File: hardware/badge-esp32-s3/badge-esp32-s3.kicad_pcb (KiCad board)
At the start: 2 copper layers, 127 x 76 mm, 0 parts

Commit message: Finish schematic, start placing parts on layout
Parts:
- added BUZZER1: MLT-5020, lcsc-lib:BUZ-SMD_L5.0-W5.5-P4.60, F.Cu at (179.0, 79.0)
- added C1: 10uF, PCM_JLCPCB:C_0603, F.Cu at (-92.3, 87.6)
- added C10: 100nF, PCM_JLCPCB:C_0603, F.Cu at (-83.7, 142.7)
- added C11: 100nF, PCM_JLCPCB:C_0603, F.Cu at (-92.3, 142.7)
- added C12: 10uF, PCM_JLCPCB:C_0603, F.Cu at (-36.4, 112.4)
- added C13: 10uF, PCM_JLCPCB:C_0603, F.Cu at (-36.4, 114.7)
- added C14: 100nF, PCM_JLCPCB:C_0603, F.Cu at (-69.2, 140.2)
- added C15: 1uF, PCM_JLCPCB:C_0402, F.Cu at (-46.6, 115.5)
- added C16: 1uF, PCM_JLCPCB:C_0402, F.Cu at (-46.6, 117.4)
- added C17: 1uF, PCM_JLCPCB:C_0402, F.Cu at (-46.6, 119.2)
- added C18: 1uF, PCM_JLCPCB:C_0603, F.Cu at (-8.72, 58.6)
- added C19: 1uF, PCM_JLCPCB:C_0603, F.Cu at (-9.82, 126.2)
- added C2: 100nF, PCM_JLCPCB:C_0603, F.Cu at (-92.3, 89.8)
- added C20: 1uF, PCM_JLCPCB:C_0603, F.Cu at (-10.7, 101.4)
- added C21: 1uF, PCM_JLCPCB:C_0603, F.Cu at (-45.8, 130.6)
- added C22: 1uF, PCM_JLCPCB:C_0603, F.Cu at (-8.72, 73.7)
- added C23: 1uF, PCM_JLCPCB:C_0603, F.Cu at (-9.82, 140.0)
- added C24: 100nF, PCM_JLCPCB:C_0603, F.Cu at (-14.5, 81.6)
- added C25: 100nF, PCM_JLCPCB:C_0603, F.Cu at (-14.5, 83.9)
- added C26: 4.7uF, PCM_JLCPCB:C_0603, F.Cu at (-14.5, 86.1)
- added C3: 1uF, PCM_JLCPCB:C_0402, F.Cu at (-44.4, 83.6)
- added C4: 1uF, PCM_JLCPCB:C_0402, F.Cu at (-44.4, 85.4)
- added C5: 10uF, PCM_JLCPCB:C_0603, F.Cu at (-22.6, 75.9)
- added C6: 10uF, PCM_JLCPCB:C_0603, F.Cu at (-22.6, 60.7)
- added C7: 10uF, PCM_JLCPCB:C_0603, F.Cu at (-36.8, 60.5)
- added C8: 1uF, PCM_JLCPCB:C_0402, F.Cu at (-44.4, 51.1)
- added C9: 1uF, PCM_JLCPCB:C_0402, F.Cu at (-44.4, 52.9)
- added CN1: B4B-PH-SM4-TB (LF)(SN), lcsc-lib:CONN-SMD_B4B-PH-SM4-TB-LF-SN, F.Cu at (-54.8, 112.8)
- added Card1: TF PUSH, lcsc-lib:TF-SMD_TF-PUSH, F.Cu at (152.9, 131.3)
- added D1: Red, PCM_JLCPCB:D_0603, F.Cu at (-40.9, 84.0)
- added D10: Red, PCM_JLCPCB:D_0603, F.Cu at (-46.5, 142.0)
- added D11: B0520W, PCM_JLCPCB:D_SOD-123, F.Cu at (-21.9, 102.7)
- added D12: Green, PCM_JLCPCB:D_0805, F.Cu at (-21.6, 112.3)
- added D2: LESD5D5.0CT1G, lcsc-lib:SOD-523_L1.2-W0.8-LS1.6-BI, F.Cu at (-17.9, 66.4)
- added D3: LESD5D5.0CT1G, lcsc-lib:SOD-523_L1.2-W0.8-LS1.6-BI, F.Cu at (-17.9, 68.5)
- added D4: LESD5D5.0CT1G, lcsc-lib:SOD-523_L1.2-W0.8-LS1.6-BI, F.Cu at (-17.9, 70.6)
- added D5: B0520W, PCM_JLCPCB:D_SOD-123, F.Cu at (-27.4, 76.5)
- added D6: LESD5D5.0CT1G, lcsc-lib:SOD-523_L1.2-W0.8-LS1.6-BI, F.Cu at (-17.9, 51.2)
- added D7: LESD5D5.0CT1G, lcsc-lib:SOD-523_L1.2-W0.8-LS1.6-BI, F.Cu at (-17.9, 53.3)
- added D8: LESD5D5.0CT1G, lcsc-lib:SOD-523_L1.2-W0.8-LS1.6-BI, F.Cu at (-17.9, 55.5)
- added D9: B0520W, PCM_JLCPCB:D_SOD-123, F.Cu at (-27.4, 61.3)
- added J1: Connector, USB-TYPE-C-16P, PCM_JLCPCB:TYPE-C-SMD_HX-TYPE-C-16PIN, F.Cu at (122.5, 69.0)
- added J2: Connector, USB-TYPE-C-16P, PCM_JLCPCB:TYPE-C-SMD_HX-TYPE-C-16PIN, F.Cu at (179.0, 69.0)
- added J3: ~, lcsc-lib:FPC-SMD_AFC01-S12FCA-00, F.Cu at (122.2, 101.5)
- added LED1: RS-3535MWAM, lcsc-lib:LED-ARRAY-SMD_L3.7-W3.5-P1.10-TL, F.Cu at (169.0, 80.0)
- added MB1: MiniBadge_Full, minibadge:MiniBadge_Full_NoEdges, F.Cu at (87.2, 65.7)
- added MB2: MiniBadge_Full, minibadge:MiniBadge_Full_NoEdges, F.Cu at (192.7, 65.7)
- added P1: PH-2A_C2319, lcsc-lib:CONN-TH_2P-P2.00_PH-2A_C2319, F.Cu at (89.0, 93.0)
- added Q1: SS8050 200-350, PCM_JLCPCB:Q_SOT-23, F.Cu at (-34.8, 52.5)
- added Q2: SS8050 200-350, PCM_JLCPCB:Q_SOT-23, F.Cu at (-34.8, 57.2)
- added Q3: HL2301A, PCM_JLCPCB:Q_SOT-23, F.Cu at (-26.3, 113.2)
- added R1: 0Ω, PCM_JLCPCB:R_0402, F.Cu at (-89.0, 87.4)
- added R10: 10kΩ, PCM_JLCPCB:R_0402, F.Cu at (-41.5, 51.1)
- added R11: 0Ω, PCM_JLCPCB:R_0402, F.Cu at (-41.5, 52.9)
- added R12: 0Ω, PCM_JLCPCB:R_0402, F.Cu at (-41.5, 54.8)
- added R13: 10kΩ, PCM_JLCPCB:R_0402, F.Cu at (-41.5, 56.6)
- added R14: 10kΩ, PCM_JLCPCB:R_0402, F.Cu at (-41.5, 58.5)
- added R15: 0Ω, PCM_JLCPCB:R_0402, F.Cu at (-38.7, 51.1)
- added R16: 0Ω, PCM_JLCPCB:R_0402, F.Cu at (-38.7, 52.9)
- added R17: 10kΩ, PCM_JLCPCB:R_0402, F.Cu at (-38.7, 54.8)
- added R18: 100Ω, PCM_JLCPCB:R_0402, F.Cu at (-28.9, 89.0)
- added R19: 5.1kΩ, PCM_JLCPCB:R_0402, F.Cu at (-50.0, 136.9)
- added R2: 5.1kΩ, PCM_JLCPCB:R_0402, F.Cu at (-44.4, 87.3)
- added R20: 100Ω, PCM_JLCPCB:R_0402, F.Cu at (-50.0, 138.7)
- added R21: 47Ω, PCM_JLCPCB:R_0402, F.Cu at (-50.0, 140.6)
- added R22: 47Ω, PCM_JLCPCB:R_0402, F.Cu at (-50.0, 142.4)
- added R23: 3296W-1-103, lcsc-lib:RES-ADJ-TH_3P-L10.0-W10.0-P2.50-L, F.Cu at (187.5, 78.5)
- added R24: 100kΩ, PCM_JLCPCB:R_0402, F.Cu at (-20.2, 105.7)
- added R25: 1kΩ, PCM_JLCPCB:R_0402, F.Cu at (-20.2, 107.6)
- added R26: 2.2kΩ, PCM_JLCPCB:R_0402, F.Cu at (-20.2, 109.4)
- added R27: 10kΩ, PCM_JLCPCB:R_0603, F.Cu at (-12.5, 58.6)
- added R28: 10kΩ, PCM_JLCPCB:R_0603, F.Cu at (-12.5, 60.8)
- added R29: 10kΩ, PCM_JLCPCB:R_0603, F.Cu at (-13.6, 126.2)
- added R3: 5.1kΩ, PCM_JLCPCB:R_0402, F.Cu at (-19.3, 75.7)
- added R30: 10kΩ, PCM_JLCPCB:R_0603, F.Cu at (-13.6, 128.5)
- added R31: 10kΩ, PCM_JLCPCB:R_0603, F.Cu at (-14.5, 101.4)
- added R32: 10kΩ, PCM_JLCPCB:R_0603, F.Cu at (-14.5, 103.6)
- added R33: 10kΩ, PCM_JLCPCB:R_0603, F.Cu at (-49.6, 130.6)
- added R34: 10kΩ, PCM_JLCPCB:R_0603, F.Cu at (-49.6, 132.8)
- added R35: 10kΩ, PCM_JLCPCB:R_0603, F.Cu at (-12.5, 73.7)
- added R36: 10kΩ, PCM_JLCPCB:R_0603, F.Cu at (-12.5, 76.0)
- added R37: 10kΩ, PCM_JLCPCB:R_0603, F.Cu at (-13.6, 140.0)
- added R38: 10kΩ, PCM_JLCPCB:R_0603, F.Cu at (-13.6, 142.3)
- added R39: 4.7kΩ, PCM_JLCPCB:R_0603, F.Cu at (-10.8, 85.9)
- added R4: 5.1kΩ, PCM_JLCPCB:R_0402, F.Cu at (-19.3, 77.6)
- added R40: 4.7kΩ, PCM_JLCPCB:R_0603, F.Cu at (-10.8, 88.2)
- added R5: 5.1kΩ, PCM_JLCPCB:R_0402, F.Cu at (-19.3, 60.5)
- added R6: 5.1kΩ, PCM_JLCPCB:R_0402, F.Cu at (-19.3, 62.4)
- added R7: 22kΩ, PCM_JLCPCB:R_0402, F.Cu at (-44.4, 54.8)
- added R8: 47kΩ, PCM_JLCPCB:R_0402, F.Cu at (-44.4, 56.6)
- added R9: 1kΩ, PCM_JLCPCB:R_0402, F.Cu at (-44.4, 58.5)
- added S1: 2765, AdafruitJoystick:SW_2765, F.Cu at (98.5, 107.5)
- added SW1: TS-1088-AR02016, lcsc-lib:SW-SMD_L3.9-W3.0-P4.45, F.Cu at (133.5, 72.0)
- added SW2: TS-1088-AR02016, lcsc-lib:SW-SMD_L3.9-W3.0-P4.45, F.Cu at (164.5, 72.0)
- added SW3: SK-12F04-G050, lcsc-lib:SW-TH_G-SWITCH_SK-12F04-G050, F.Cu at (210.5, 96.5)
- added SW4: TS665CJ, lcsc-lib:SW-TH_4P-L6.0-W6.0-P4.50-LS6.5, F.Cu at (206.0, 123.5)
- added SW5: TS665CJ, lcsc-lib:SW-TH_4P-L6.0-W6.0-P4.50-LS6.5, F.Cu at (197.2, 115.5)
- added SW6: TS665CJ, lcsc-lib:SW-TH_4P-L6.0-W6.0-P4.50-LS6.5, F.Cu at (189.0, 123.8)
- added SW7: TS665CJ, lcsc-lib:SW-TH_4P-L6.0-W6.0-P4.50-LS6.5, F.Cu at (111.8, 129.8)
- added SW8: TS665CJ, lcsc-lib:SW-TH_4P-L6.0-W6.0-P4.50-LS6.5, F.Cu at (99.2, 126.2)
- added SW9: TS665CJ, lcsc-lib:SW-TH_4P-L6.0-W6.0-P4.50-LS6.5, F.Cu at (197.5, 132.0)
- added U1: ESP32-S3-MINI-1-N8, RF_Module:ESP32-S2-MINI-1, F.Cu at (150.7, 75.5)
- added U10: FH2.54-09-02PZD, lcsc-lib:HDR-TH_2P-P2.54-V-M-5, F.Cu at (-66.3, 102.7)
- added U11: FH2.54-09-04PZD, lcsc-lib:HDR-TH_4P-P2.54-V-F, F.Cu at (-55.6, 94.8)
- added U12: FH2.54-09-03PZD, lcsc-lib:HDR-TH_3P-P2.54-V-F, F.Cu at (-45.0, 102.3)
- added U13: FH2.54-09-02PZD, lcsc-lib:HDR-TH_2P-P2.54-V-M-5, F.Cu at (-109.0, 104.0)
- added U14: FH2.54-09-04PZD, lcsc-lib:HDR-TH_4P-P2.54-V-F, F.Cu at (-55.6, 98.6)
- added U15: FH2.54-09-04PZD, lcsc-lib:HDR-TH_4P-P2.54-V-F, F.Cu at (-55.6, 102.4)
- added U16: FH2.54-09-04PZD, lcsc-lib:HDR-TH_4P-P2.54-V-F, F.Cu at (-55.6, 106.2)
- added U17: FH2.54-09-02PZD, lcsc-lib:HDR-TH_2P-P2.54-V-M-5, F.Cu at (-11.5, 110.0)
- added U18: MMA8452QR1_C11360, lcsc-lib:QFN-16_L3.0-W3.0-P0.50-TL_MMA8452QR1, F.Cu at (198.5, 93.8)
- added U19: FH2.54-09-02PZD, lcsc-lib:HDR-TH_2P-P2.54-V-M-5, F.Cu at (-66.3, 115.7)
- added U2: NCP167BMX330TBG, lcsc-lib:XDFN-4_L1.0-W1.0-P0.65-BL-EP, F.Cu at (-41.4, 86.5)
- added U3: CP2102N-A02-GQFN28R, lcsc-lib:QFN-28_L5.0-W5.0-P0.50-TL-EP3.3, F.Cu at (122.1, 78.5)
- added U4: TP4056, PCM_JLCPCB:ESOP-8_L4.9-W3.9-P1.27-LS6.0-BL-EP, F.Cu at (102.8, 93.0)
- added U5: FH2.54-09-02PZD, lcsc-lib:HDR-TH_2P-P2.54-V-M-5, F.Cu at (-28.3, 131.0)
- added U6: ZX-SH1.0-4PWT, lcsc-lib:CONN-SMD_4P-P1.00_MEGASTAR_ZX-SH1.0-4PWT, F.Cu at (-44.2, 111.2)
- added U7: FH2.54-09-02PZD, lcsc-lib:HDR-TH_2P-P2.54-V-M-5, F.Cu at (-90.8, 113.5)
- added U8: FH2.54-09-03PZD, lcsc-lib:HDR-TH_3P-P2.54-V-F, F.Cu at (-45.0, 94.8)
- added U9: FH2.54-09-03PZD, lcsc-lib:HDR-TH_3P-P2.54-V-F, F.Cu at (-45.0, 98.6)

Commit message: Layout placed
I've completed the PCB layout and am handing it off for trace routing. It's been a while since I last did this, so while I did my best to optimize placement, there may be areas where space is tight. Feel free to adjust component positioning as needed to make routing easier.

Feedback is welcome—I wish I had more time to do the traces myself since that would be a valuable learning opportunit.
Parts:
- moved C3 250.9 mm to (206.4, 91.1), turned to -90 degrees
- moved C4 248.0 mm to (203.5, 93.2)
- moved R2 245.8 mm to (201.4, 91.1), turned to 90 degrees
- moved U2 244.9 mm to (203.5, 91.1)
- moved D1 244.5 mm to (203.6, 88.6), turned to 180 degrees
- moved U13 241.2 mm to (129.8, 137.7)
- moved C11 239.3 mm to (137.8, 77.0), turned to 90 degrees
- moved U12 234.3 mm to (189.3, 103.3), turned to 90 degrees
- moved U19 234.0 mm to (164.6, 77.7), turned to 180 degrees
- moved C10 232.4 mm to (137.8, 72.4), turned to 90 degrees
- moved U7 231.0 mm to (138.9, 137.7), turned to 180 degrees
- moved U9 228.8 mm to (183.8, 103.2), turned to 90 degrees
- moved U11 228.7 mm to (173.0, 102.1), turned to 90 degrees
- moved C14 227.6 mm to (157.8, 123.6)
- moved R28 225.5 mm to (205.4, 119.0), turned to 180 degrees
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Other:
- board outline removed

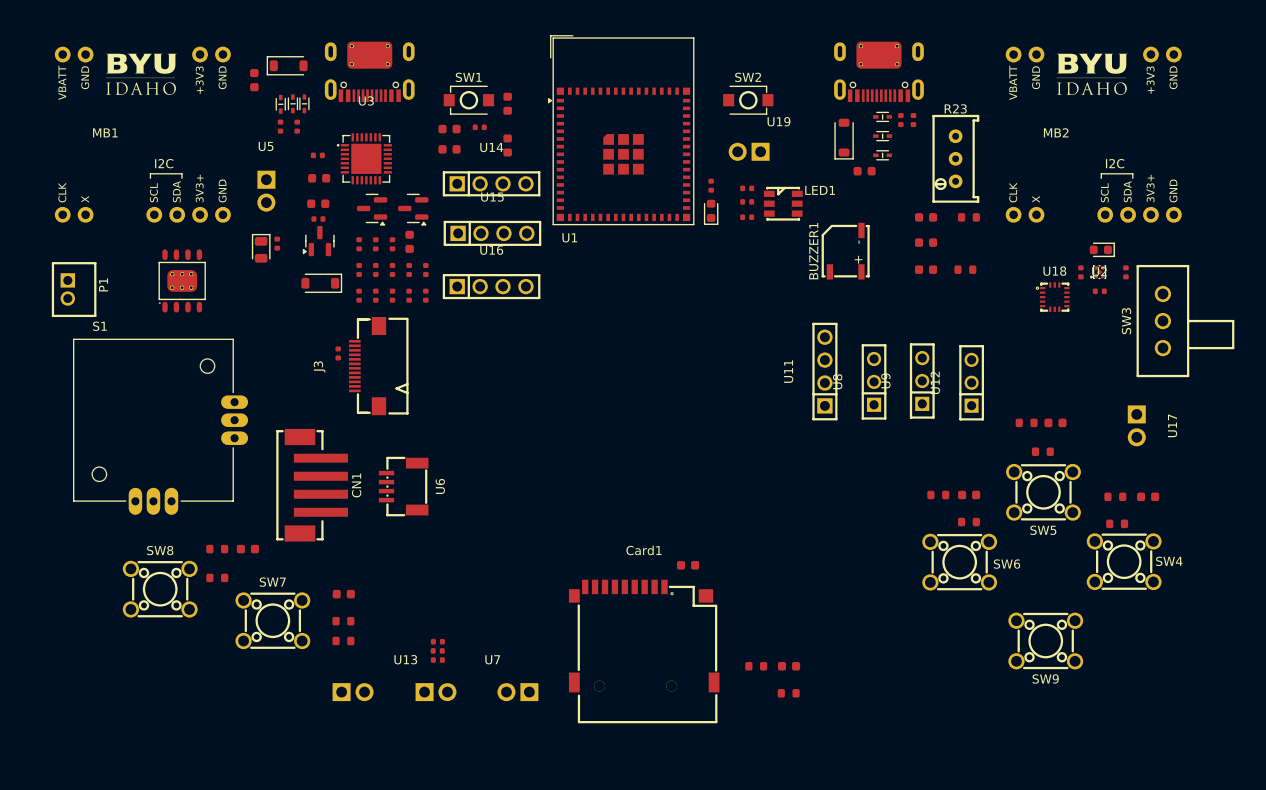
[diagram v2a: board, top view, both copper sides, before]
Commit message: Add nice silkscreens
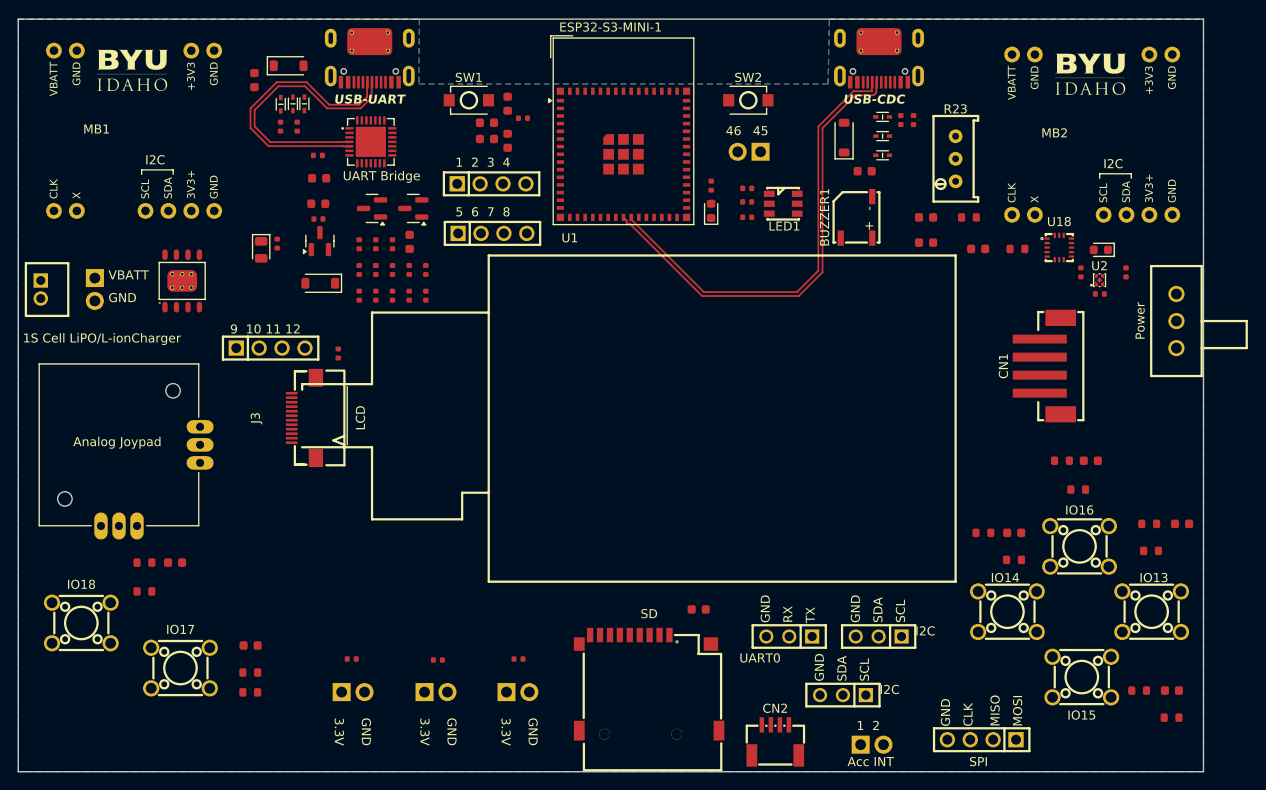
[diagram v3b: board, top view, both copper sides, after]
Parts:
- added LCD: OLED-SMD_HS20HS072RX, lcsc-lib:OLED-SMD_HS20HS072RX, F.Cu at (117.5, 107.2)
- moved CN1 83.1 mm to (198.0, 101.5), turned to 90 degrees
- moved CN2 50.1 mm to (167.5, 143.0), turned to 0 degrees
- moved U17 46.0 mm to (178.2, 143.5), turned to 0 degrees
- moved U11 44.4 mm to (190.4, 142.9), turned to 180 degrees
- moved R37 42.6 mm to (207.9, 137.5)
- moved R38 42.6 mm to (211.5, 140.5)
- moved C23 42.6 mm to (211.5, 137.5)
- moved U9 35.9 mm to (175.0, 138.0), turned to 180 degrees
- moved U12 30.0 mm to (179.0, 131.5), turned to 180 degrees
- moved U8 29.8 mm to (169.0, 131.5), turned to 180 degrees
- moved U16 25.4 mm to (111.5, 99.5)
- moved U5 21.9 mm to (92.0, 93.0)
- moved C21 11.8 mm to (109.3, 132.5)
- moved R33 11.8 mm to (109.2, 137.7)
- moved R34 11.8 mm to (109.2, 135.5)
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- renumbered U6 to CN2, SW4 to IO13, SW6 to IO14, SW9 to IO15, SW5 to IO16, SW7 to IO17, SW8 to IO18, SW3 to Power, Card1 to SD
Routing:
- net /ESP_USB-: track 0.00 -> 51.8 mm
- net /ESP_USB+: track 0.00 -> 49.9 mm
- net /UART Interface/USB_DN: track 0.00 -> 31.2 mm
- net /UART Interface/USB_DP: track 0.00 -> 30.4 mm
- added copper zone on B.Cu, net GND
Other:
- board outline added: 131.5 x 83.5 mm
- board text added: "1 2"
- board text added: "1 2 3 4"
- board text added: "1S Cell LiPO/L-ionCharger"
- board text added: "3.3V"
- board text added: "45"
- board text added: "46"
- board text added: "5 6 7 8"
- board text added: "9 10 11 12"
- board text added: "Acc INT"
- board text added: "Analog Joypad"
- board text added: "CLK"
- board text added: "ESP32-S3-MINI-1"
- board text added: "GND"
- board text added: "I2C"
- board text added: "MISO"
- board text added: "MOSI"
- board text added: "RX"
- board text added: "SCL"
- board text added: "SDA"
- board text added: "SPI"
- board text added: "TX"
- board text added: "UART Bridge"
- board text added: "UART0"
- board text added: "USB-CDC"
- board text added: "USB-UART"
- board text added: "VBATT"

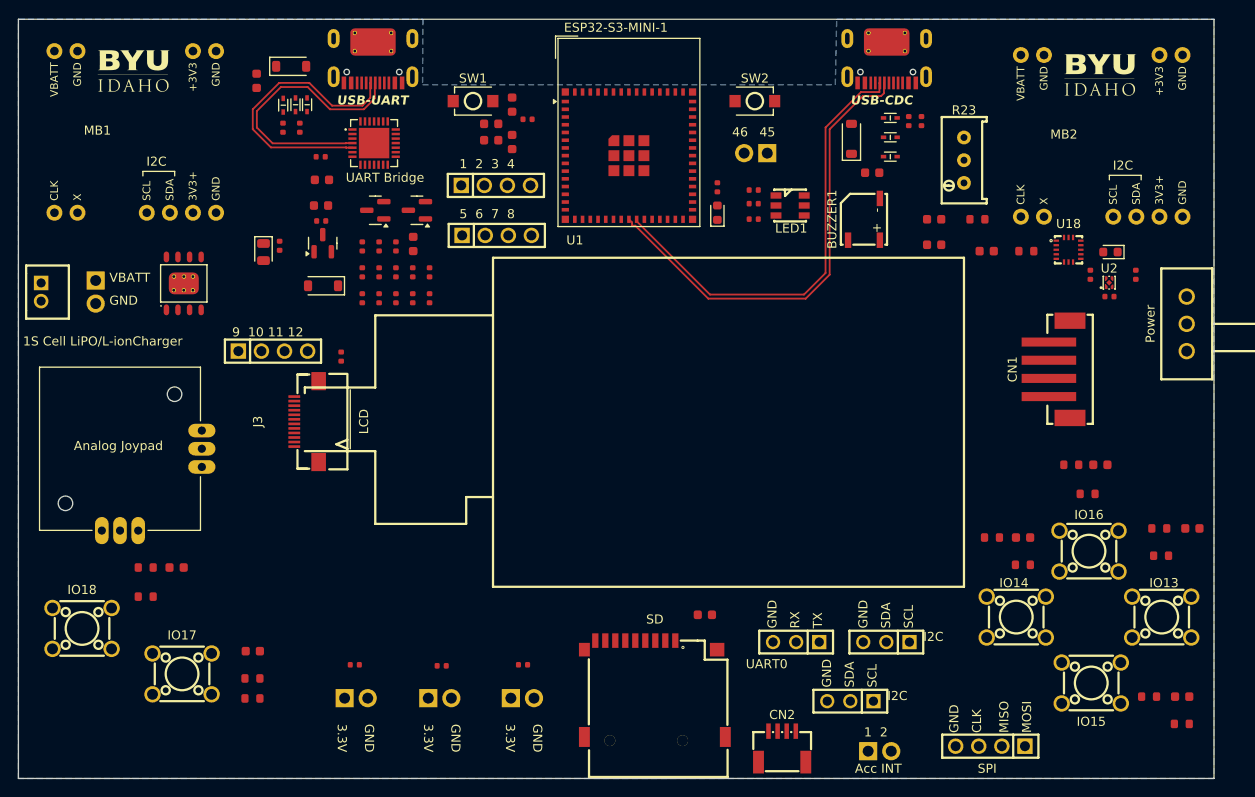
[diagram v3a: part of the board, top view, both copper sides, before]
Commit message: Start routing stuff Used free route, so it's not ideal
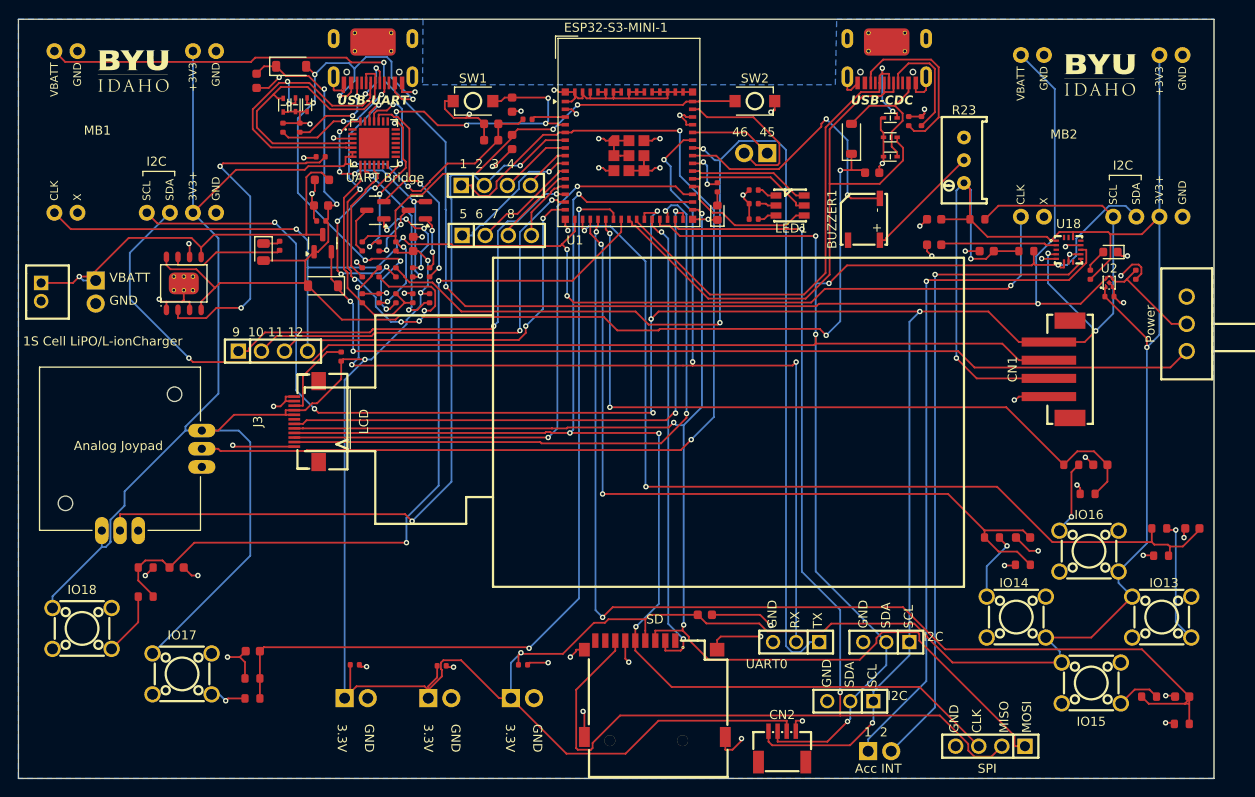
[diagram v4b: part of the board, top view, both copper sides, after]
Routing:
- net +3.3V: track 0.00 -> 542.6 mm, vias 0 -> 9
- net /GPIO21: track 0.00 -> 251.7 mm, vias 0 -> 9
- net /GPIO47: track 0.00 -> 247.6 mm, vias 0 -> 6
- net GND: track 0.00 -> 212.6 mm, vias 0 -> 61
- net +4V: track 0.00 -> 182.0 mm, vias 0 -> 3
- net /GPIO36: track 0.00 -> 146.9 mm, vias 0 -> 4
- net /GPIO35: track 0.00 -> 142.4 mm, vias 0 -> 3
- net /USB_5V: track 0.00 -> 142.1 mm, vias 0 -> 4
- net /GPIO12: track 0.00 -> 138.6 mm, vias 0 -> 5
- net /GPIO34.: track 0.00 -> 135.2 mm, vias 0 -> 2
- net /U0TX: track 0.00 -> 127.4 mm, vias 0 -> 2
- net /GPIO15: track 0.00 -> 122.5 mm, vias 0 -> 2
- net /U0RX: track 0.00 -> 120.0 mm, vias 0 -> 5
- net /GPIO1: track 0.00 -> 120.0 mm, vias 0 -> 2
- net Net-(Q3-S): track 0.00 -> 105.1 mm, vias 0 -> 2
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
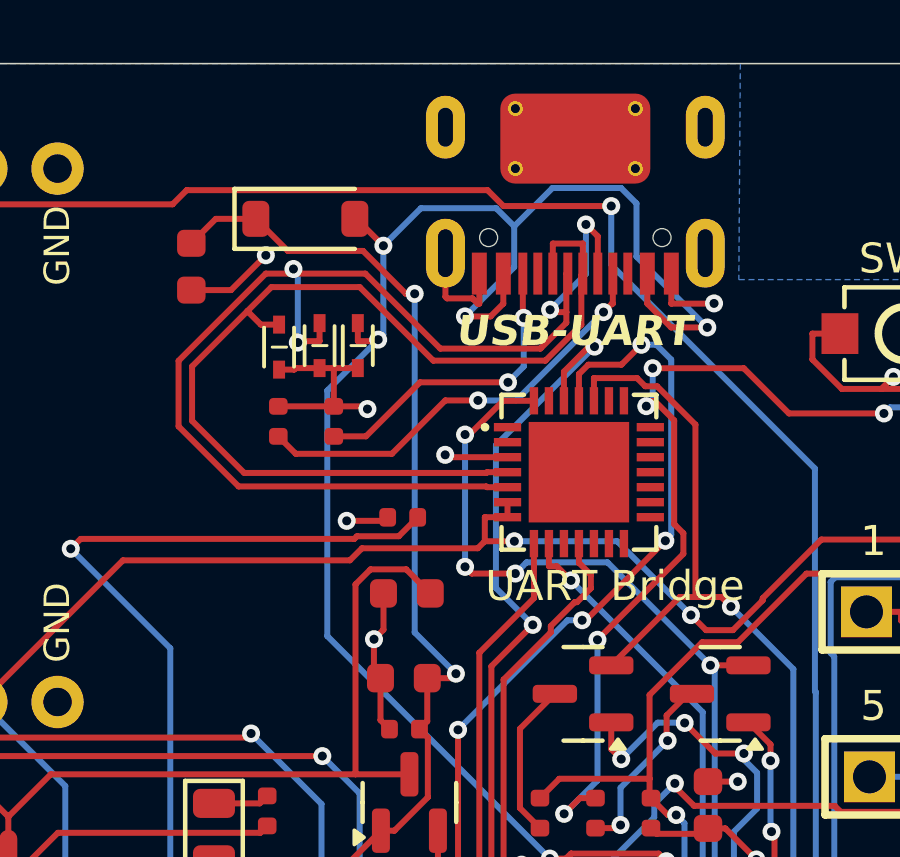
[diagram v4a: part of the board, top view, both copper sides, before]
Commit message: Fix some DRC errors
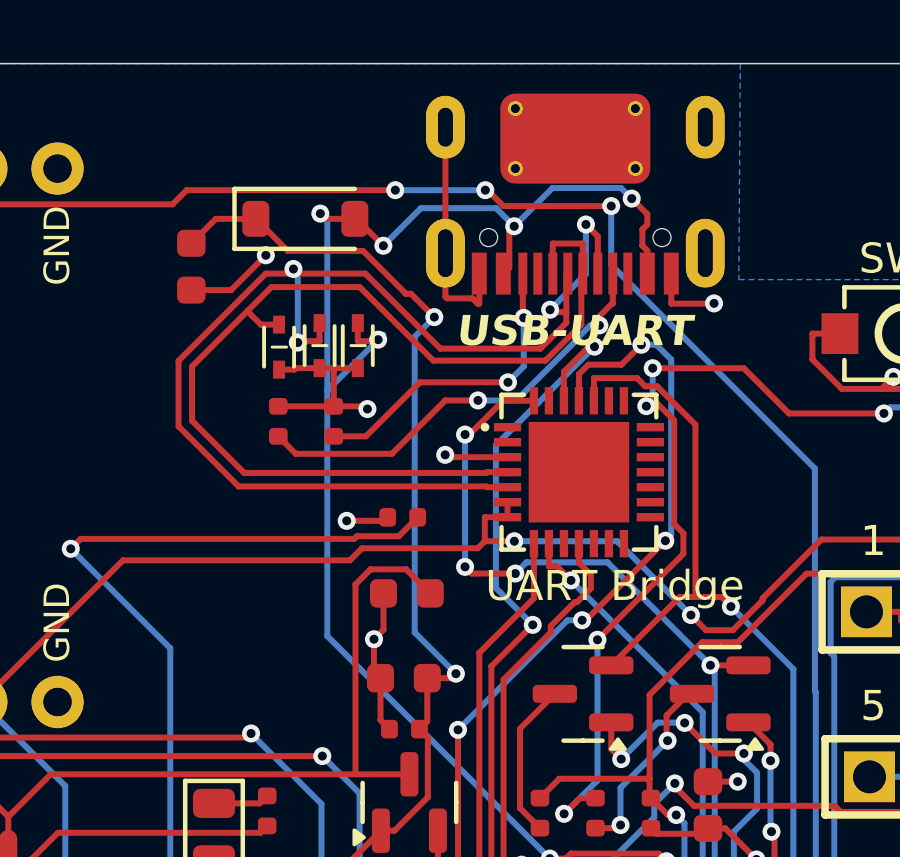
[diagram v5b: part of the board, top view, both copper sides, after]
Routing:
- net /VBUS: track 63.5 -> 57.5 mm, vias 7 -> 8
- net GND: track 212.6 -> 216.8 mm
- net +4V: vias 3 -> 5
